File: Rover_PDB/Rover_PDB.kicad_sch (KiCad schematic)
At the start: 0 parts

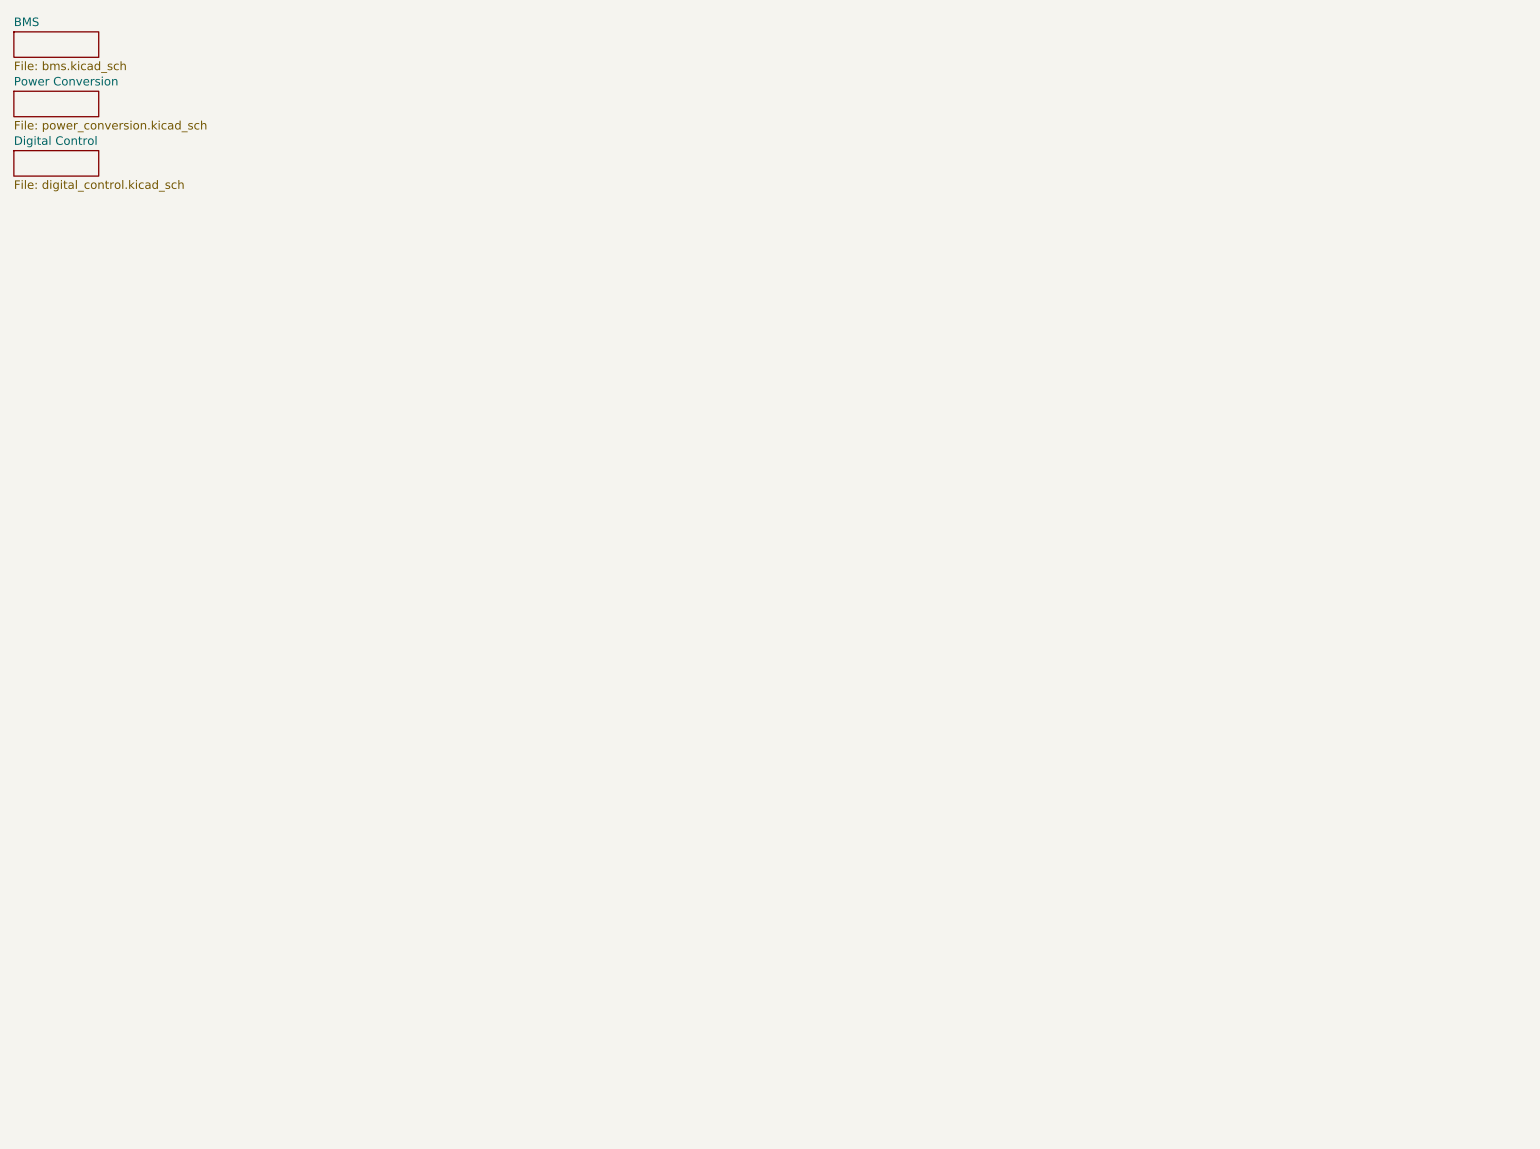
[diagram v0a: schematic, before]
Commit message: move stuff around
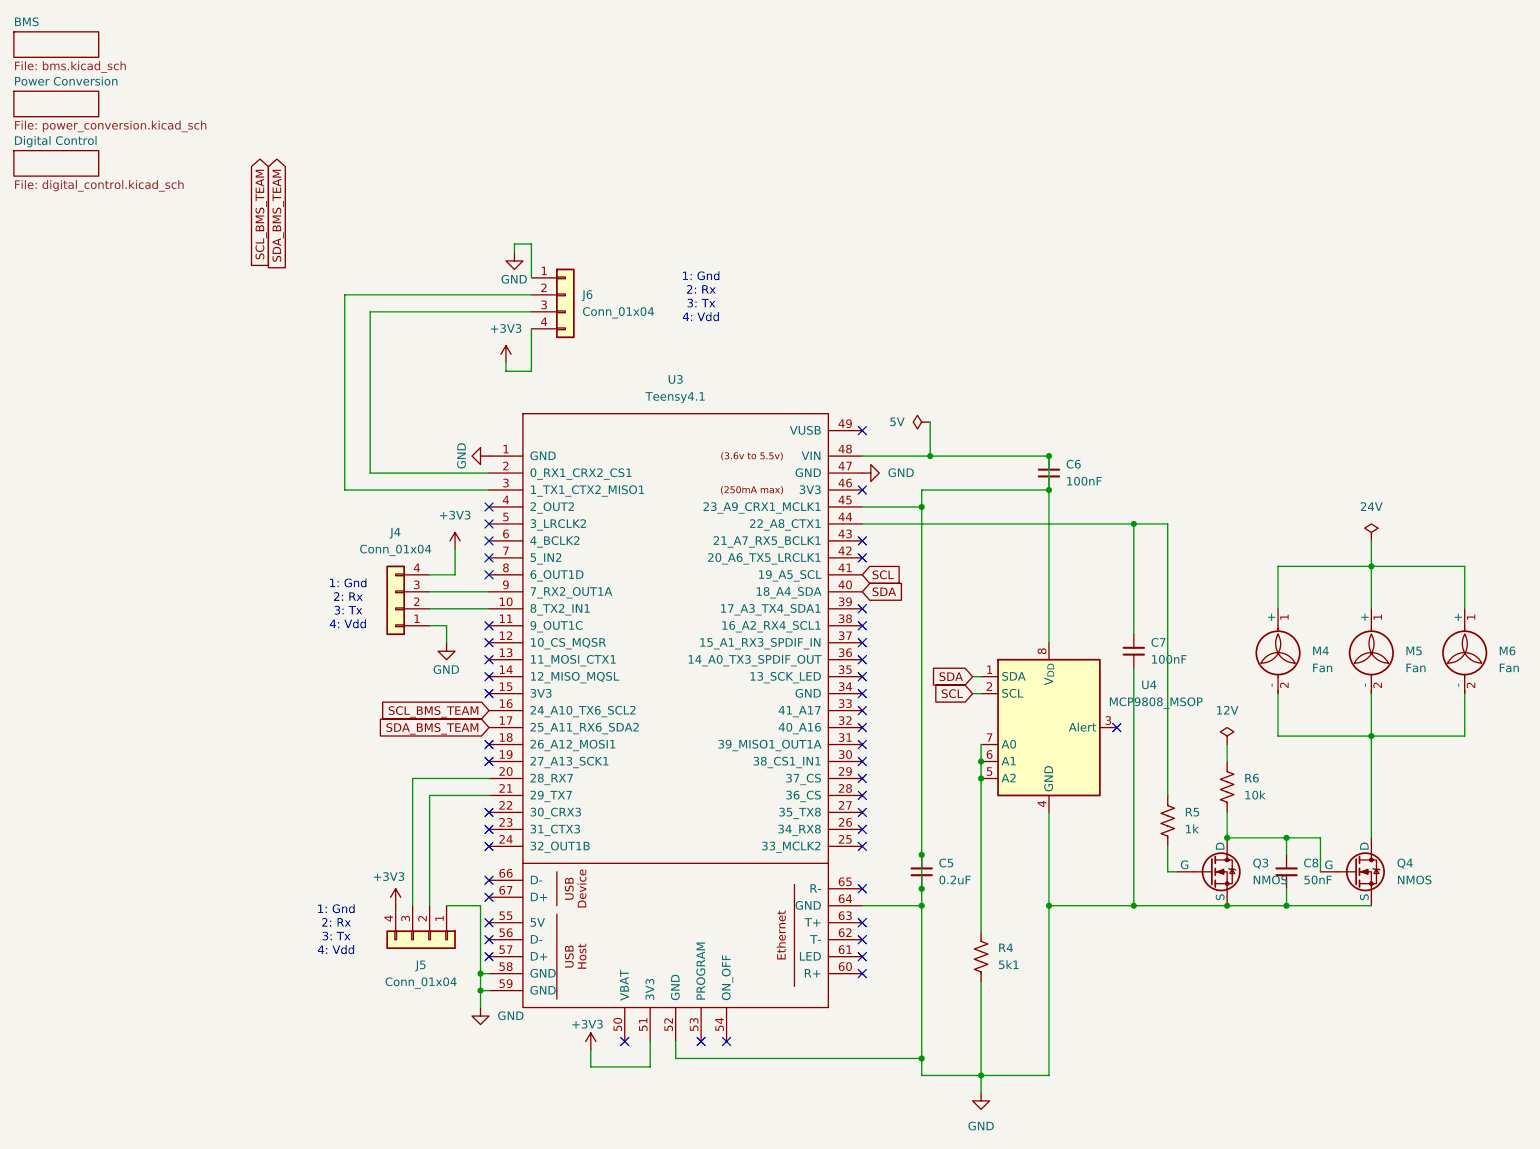
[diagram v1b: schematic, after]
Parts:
- added C5: 0.2uF, Capacitor_SMD:C_01005_0402Metric, symbol Device:C_Small
- added C6, C7: 100nF, Capacitor_SMD:C_01005_0402Metric, symbol Device:C_Small
- added C8: 50nF, Capacitor_SMD:C_01005_0402Metric, symbol Device:C_Small
- added J4, J5, J6: Conn_01x04, Connector_Wago:Wago_734-134_1x04_P3.50mm_Vertical, symbol Connector_Generic:Conn_01x04
- added M4, M5, M6: Fan, Connector_JST:JST_XH_B2B-XH-A_1x02_P2.50mm_Vertical, symbol Motor:Fan
- added Q3, Q4: NMOS, Package_TO_SOT_THT:TO-220-3_Vertical, symbol Simulation_SPICE:NMOS
- added R4: 5k1, Resistor_SMD:R_01005_0402Metric, symbol Device:R_US
- added R5: 1k, Resistor_SMD:R_01005_0402Metric, symbol Device:R_US
- added R6: 10k, Resistor_SMD:R_01005_0402Metric, symbol Device:R_US
- added U3: Teensy4.1, teensy:Teensy41, symbol teensy:Teensy4.1
- added U4: MCP9808_MSOP, Package_SO:MSOP-8_3x3mm_P0.65mm, symbol Sensor_Temperature:MCP9808_MSOP
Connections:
- new net: R4.1, U4.5 (A2), U4.6 (A1), U4.7 (A0)
- new net: J4.2 (Pin_2), U3.10 (8_TX2_IN1)
- new net: J4.3 (Pin_3), U3.9 (7_RX2_OUT1A)
- new net: M4.2 (-), M5.2 (-), M6.2 (-), Q4.1 (D)
- new net: C8.1, Q3.1 (D), Q4.2 (G), R6.2
- new net: C7.1, R5.1, U3.44 (22_A8_CTX1)
- new net: M4.1 (+), M5.1 (+), M6.1 (+)
- new net: J6.3 (Pin_3), U3.2 (0_RX1_CRX2_CS1)
- new net: J5.3 (Pin_3), U3.20 (28_RX7)
- new net: J5.2 (Pin_2), U3.21 (29_TX7)
- new net: J6.2 (Pin_2), U3.3 (1_TX1_CTX2_MISO1)
- new net: Q3.2 (G), R5.2
- new net +3V3: J4.4 (Pin_4), J5.4 (Pin_4), J6.4 (Pin_4), U3.51 (3V3)
- new net GND: C5.1, C5.2, C6.1, C6.2, C7.2, C8.2, J4.1 (Pin_1), J5.1 (Pin_1), J6.1 (Pin_1), Q3.3 (S), Q4.3 (S), R4.2, U3.1 (GND), U3.45 (23_A9_CRX1_MCLK1), U3.47 (GND), U3.48 (VIN), U3.52 (GND), U3.58 (GND), U3.59 (GND), U3.64 (GND), U4.4 (GND), U4.8 (V_{DD})
- new net SCL: U3.41 (19_A5_SCL), U4.2 (SCL)
- new net SCL_BMS_TEAM: U3.16 (24_A10_TX6_SCL2)
- new net SDA: U3.40 (18_A4_SDA), U4.1 (SDA)
- new net SDA_BMS_TEAM: U3.17 (25_A11_RX6_SDA2)
- no-connect marks 0 -> 48
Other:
- note added: "1: Gnd 2: Rx 3: Tx 4: Vdd"
